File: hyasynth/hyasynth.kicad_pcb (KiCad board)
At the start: 2 copper layers, 43 parts, among them J1 Conn_01x04_Male, J2 Conn_01x03_Male, J3 Conn_01x09_Male, J4 Conn_01x05_Male, SW1 Power Switch, SW10 G# Ab, SW11 A, SW12 A# Bb, SW13 B, SW14 C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

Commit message: started laying out pcb
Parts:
- added J5: Conn_01x02_Male, Connector_PinHeader_2.54mm:PinHeader_1x02_P2.54mm_Vertical, F.Cu at (191.0, 32.0)
- added R5: R, Resistor_SMD:R_0805_2012Metric_Pad1.20x1.40mm_HandSolder, F.Cu at (192.0, 35.0)
- BT1, BT2, C6, C8: moved to B.Cu
- moved J1 243.4 mm to (257.0, 15.2)
- moved SW1 217.1 mm to (258.0, 54.0), turned to 180 degrees
- moved BT1 209.8 mm to (236.0, 38.0), turned to 180 degrees
- moved SW18 209.0 mm to (250.0, 39.0)
- moved J3 200.9 mm to (225.8, 32.0), turned to 90 degrees
- moved SW16 199.2 mm to (249.0, 58.0), turned to 90 degrees
- moved SW13 198.9 mm to (246.0, 82.0), turned to 90 degrees
- moved R1 194.8 mm to (251.0, 33.0)
- moved SW12 194.5 mm to (240.0, 73.0), turned to 90 degrees
- moved SW14 192.7 mm to (256.0, 82.0), turned to 90 degrees
- moved R2 190.3 mm to (255.0, 32.0)
- moved J2 188.7 mm to (210.0, 36.0)
- moved SW9 183.1 mm to (219.0, 82.0), turned to 90 degrees
- moved C2 182.5 mm to (229.0, 46.0), turned to 90 degrees
- moved U1 179.4 mm to (236.0, 43.0)
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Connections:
- C10 pad 2: Net-(C10-Pad2) -> /V_pot_in
- U3 pad 3: Net-(C10-Pad2) -> /V_pot_out
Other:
- board outline added: 100 x 60 mm

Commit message: Did very little work
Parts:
- moved J1 41.6 mm to (219.0, 32.0)
- moved C3 5.06 mm to (222.4, 49.0)
- moved C10 1.51 mm to (198.8, 32.0)
- moved R5 0.42 mm to (192.3, 35.3)
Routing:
- net GND: track 0.00 -> 42.6 mm
- net /A_in: track 0.00 -> 37.0 mm
- net /DAC: track 0.00 -> 30.5 mm
- net /SPK-: track 0.00 -> 13.7 mm
- net /D_in: track 0.00 -> 13.1 mm
- net /SPK+: track 0.00 -> 10.3 mm
- net /V_pot_in: track 0.00 -> 7.66 mm
- net VDD: track 0.00 -> 4.92 mm
- net Net-(C11-Pad2): track 0.00 -> 3.86 mm
- net /V_pot_out: track 0.00 -> 3.42 mm
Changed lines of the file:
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@@
   )
   (setup
+    (stackup
+      (layer "F.SilkS" (type "Top Silk Screen"))
+      (layer "F.Paste" (type "Top Solder Paste"))
+      (layer "F.Mask" (type "Top Solder Mask") (thickness 0.01))
+      (layer "F.Cu" (type "copper") (thickness 0.035))
+      (layer "dielectric 1" (type "core") (thickness 1.51) (material "FR4") (epsilon_r 4.5) (loss_tangent 0.02))
+      (layer "B.Cu" (type "copper") (thickness 0.035))
+      (layer "B.Mask" (type "Bottom Solder Mask") (thickness 0.01))
+      (layer "B.Paste" (type "Bottom Solder Paste"))
+      (layer "B.SilkS" (type "Bottom Silk Screen"))
+      (copper_finish "None")
+      (dielectric_constraints no)
+    )
     (pad_to_mask_clearance 0)
+    (grid_origin 189.2 46.2)
     (pcbplotparams
       (layerselection 0x00010fc_ffffffff)
@@
   )
   (footprint "Connector_PinSocket_2.54mm:PinSocket_1x04_P2.54mm_Vertical" (layer "F.Cu")
-    (at 257.025 15.2)
+    (at 219 32)
     (descr "Through hole straight socket strip, 1x04, 2.54mm pitch, single row (from Kicad 4.0.7), script generated")
     (tags "Through hole socket strip THT 1x04 2.54mm single row")
@@
   )
   (footprint "Capacitor_Tantalum_SMD:CP_EIA-6032-28_Kemet-C_Pad2.25x2.35mm_HandSolder" (layer "F.Cu")
-    (at 225.55 53)
+    (at 222.45 49)
     (descr "Tantalum Capacitor SMD Kemet-C (6032-28 Metric), IPC_7351 nominal, (Body size from: http://www.kemet.com/Lists/ProductCatalog/Attachments/253/KEM_TC101_STD.pdf), generated with kicad-footprint-generator")
     (tags "capacitor tantalum")
@@
   )
   (footprint "Resistor_SMD:R_0805_2012Metric_Pad1.20x1.40mm_HandSolder" (layer "F.Cu")
-    (at 192 35 180)
+    (at 192.3 35.3 180)
     (descr "Resistor SMD 0805 (2012 Metric), square (rectangular) end terminal, IPC_7351 nominal with elongated pad for handsoldering. (Body size source: IPC-SM-782 page 72, https://www.pcb-3d.com/wordpress/wp-content/uploads/ipc-sm-782a_amendment_1_and_2.pdf), generated with kicad-footprint-generator")
     (tags "resistor handsolder")
@@
   )
   (footprint "Capacitor_SMD:C_0805_2012Metric_Pad1.18x1.45mm_HandSolder" (layer "F.Cu")
-    (at 199.9625 33 180)
+    (at 198.8375 32 180)
     (descr "Capacitor SMD 0805 (2012 Metric), square (rectangular) end terminal, IPC_7351 nominal with elongated pad for handsoldering. (Body size source: IPC-SM-782 page 76, https://www.pcb-3d.com/wordpress/wp-content/uploads/ipc-sm-782a_amendment_1_and_2.pdf, https://docs.google.com/spreadsheets/d/1BsfQQcO9C6DZCsRaXUlFlo91Tg2WpOkGARC1WS5S8t0/edit?usp=sharing), generated with kicad-footprint-generator")
     (tags "capacitor handsolder")
@@
   )
   (gr_rect (start 260 30) (end 160 90) (layer "Edge.Cuts") (width 0.1) (fill none))
+  (segment (start 195.382731 40.675) (end 191.7 44.357731) (width 0.2032) (layer "F.Cu") (net 3))
+  (segment (start 189.3 45.3375) (end 185.9625 42) (width 0.2032) (layer "F.Cu") (net 3))
+  (segment (start 196.46 49.3) (end 198.16 51) (width 0.2032) (layer "F.Cu") (net 3))
+  (segment (start 191.348889 52.151111) (end 189.851111 52.151111) (width 0.2032) (layer "F.Cu") (net 3))
+  (segment (start 201 38) (end 198.325 40.675) (width 0.2032) (layer "F.Cu") (net 3))
+  (segment (start 189.3 51.6) (end 189.3 45.3375) (width 0.2032) (layer "F.Cu") (net 3))
+  (segment (start 191.348889 52.151111) (end 193.556807 52.151111) (width 0.2032) (layer "F.Cu") (net 3))
+  (segment (start 196.1125 40.675) (end 195.382731 40.675) (width 0.2032) (layer "F.Cu") (net 3))
+  (segment (start 191.7 44.357731) (end 191.7 51.8) (width 0.2032) (layer "F.Cu") (net 3))
+  (segment (start 194.231111 51.476807) (end 194.231111 50.168889) (width 0.2032) (layer "F.Cu") (net 3))
+  (segment (start 191.7 51.8) (end 191.348889 52.151111) (width 0.2032) (layer "F.Cu") (net 3))
+  (segment (start 193.556807 52.151111) (end 194.231111 51.476807) (width 0.2032) (layer "F.Cu") (net 3))
+  (segment (start 195.1 49.3) (end 196.46 49.3) (width 0.2032) (layer "F.Cu") (net 3))
+  (segment (start 189.851111 52.151111) (end 189.3 51.6) (width 0.2032) (layer "F.Cu") (net 3))
+  (segment (start 194.231111 50.168889) (end 195.1 49.3) (width 0.2032) (layer "F.Cu") (net 3))
+  (segment (start 198.325 40.675) (end 196.1125 40.675) (width 0.2032) (layer "F.Cu") (net 3))
+  (segment (start 196.1875 41.25) (end 196.1125 41.325) (width 0.2032) (layer "F.Cu") (net 25))
+  (segment (start 201 41.25) (end 196.1875 41.25) (width 0.2032) (layer "F.Cu") (net 25))
+  (segment (start 201.4 47.14) (end 201.4 50.3) (width 0.2032) (layer "F.Cu") (net 26))
+  (segment (start 210 38.54) (end 201.4 47.14) (width 0.2032) (layer "F.Cu") (net 26))
+  (segment (start 198.9 52.8) (end 189.8 52.8) (width 0.2032) (layer "F.Cu") (net 26))
+  (segment (start 201.4 50.3) (end 198.9 52.8) (width 0.2032) (layer "F.Cu") (net 26))
+  (segment (start 189.8 52.8) (end 188 51) (width 0.2032) (layer "F.Cu") (net 26))
+  (segment (start 210 41.08) (end 210 43.1) (width 0.2032) (layer "F.Cu") (net 33))
+  (segment (start 210 43.1) (end 199.5 53.6) (width 0.2032) (layer "F.Cu") (net 33))
+  (segment (start 199.5 53.6) (end 181.6 53.6) (width 0.2032) (layer "F.Cu") (net 33))
+  (segment (start 181.6 53.6) (end 180 52) (width 0.2032) (layer "F.Cu") (net 33))
+  (segment (start 210 33.8) (end 210 36) (width 0.2032) (layer "F.Cu") (net 36))
+  (segment (start 199.875 32) (end 208.2 32) (width 0.2032) (layer "F.Cu") (net 36))
+  (segment (start 208.2 32) (end 210 33.8) (width 0.2032) (layer "F.Cu") (net 36))
+  (segment (start 193.54 32) (end 197.8 32) (width 0.508) (layer "F.Cu") (net 37))
+  (segment (start 193.54 35.06) (end 193.3 35.3) (width 0.508) (layer "F.Cu") (net 37))
+  (segment (start 193.54 32) (end 193.54 35.06) (width 0.508) (layer "F.Cu") (net 37))
+  (segment (start 191.8875 41.975) (end 188.0625 41.975) (width 0.2032) (layer "F.Cu") (net 38))
+  (segment (start 188.0625 41.975) (end 188.0375 42) (width 0.2032) (layer "F.Cu") (net 38))
+  (segment (start 190.54 44.867731) (end 190.54 51) (width 0.2032) (layer "F.Cu") (net 39))
+  (segment (start 196.1125 40.025) (end 195.382731 40.025) (width 0.2032) (layer "F.Cu") (net 39))
+  (segment (start 195.382731 40.025) (end 190.54 44.867731) (width 0.2032) (layer "F.Cu") (net 39))
+  (segment (start 193.08 51) (end 193.08 45.0075) (width 0.2032) (layer "F.Cu") (net 40))
+  (segment (start 193.08 45.0075) (end 196.1125 41.975) (width 0.2032) (layer "F.Cu") (net 40))
+  (segment (start 191 35) (end 191.3 35.3) (width 0.508) (layer "F.Cu") (net 48))
+  (segment (start 191 32) (end 191 35) (width 0.508) (layer "F.Cu") (net 48))
 )

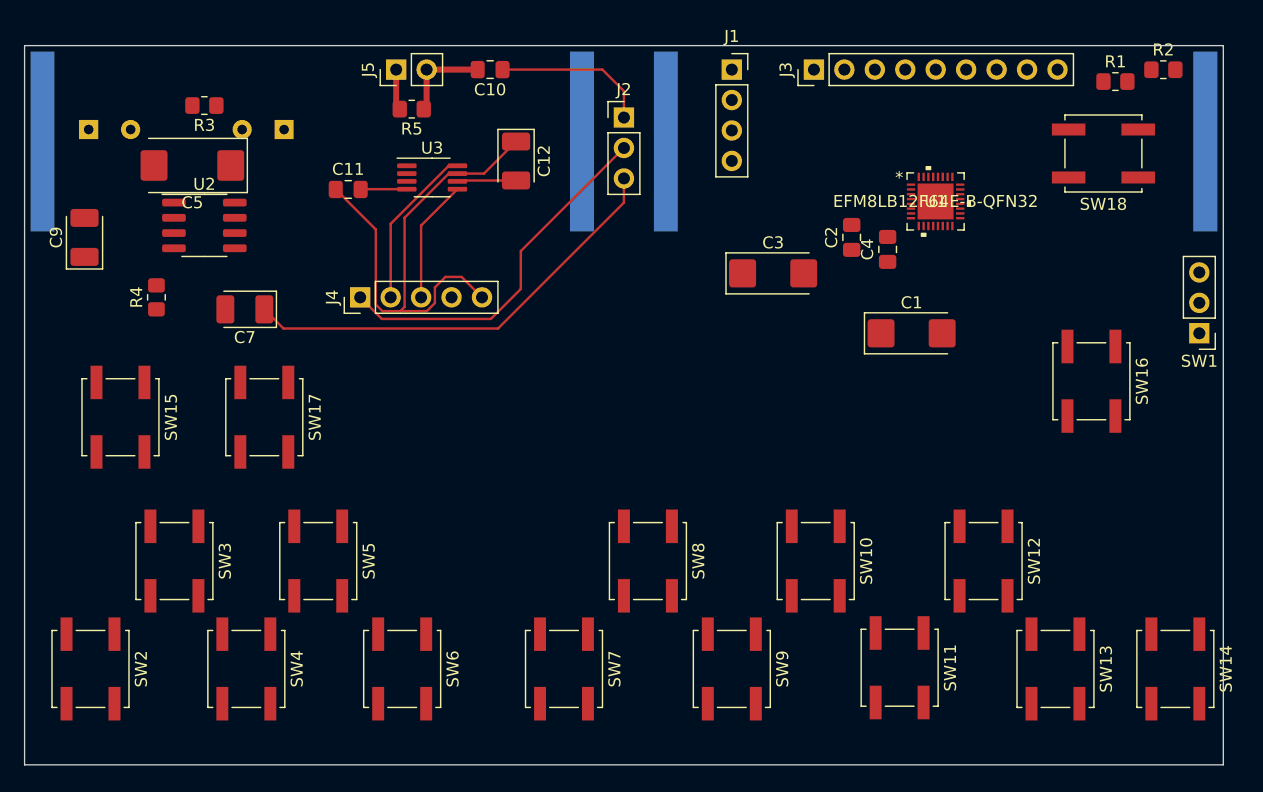
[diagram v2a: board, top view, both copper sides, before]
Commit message: set battery positions, adjusted for caps
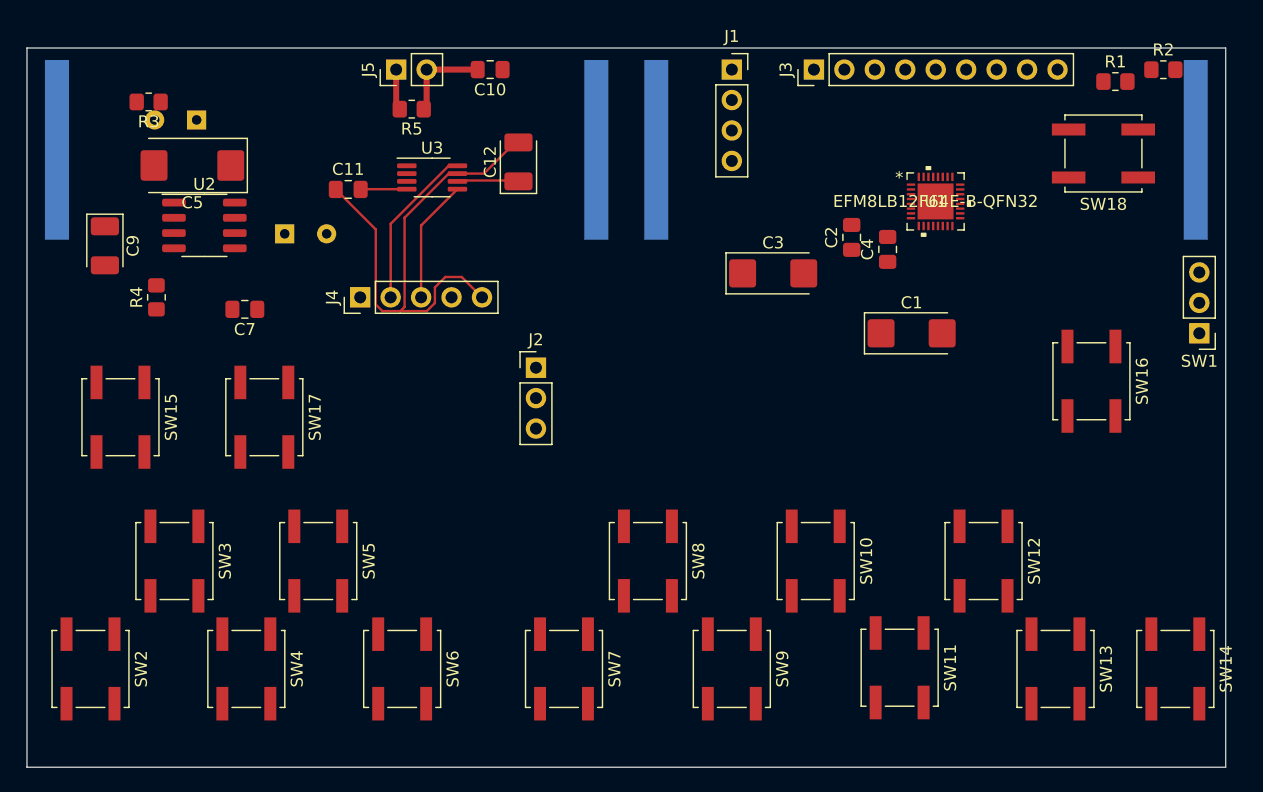
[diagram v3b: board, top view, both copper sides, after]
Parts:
- C12, C9: footprint Capacitor_Tantalum_SMD:CP_EIA-3528-21_Kemet-B_Pad1.50x2.35mm_HandSolder -> Capacitor_Tantalum_SMD:CP_EIA-3528-12_Kemet-T_Pad1.50x2.35mm_HandSolder
- C7: value 1u -> 0.1u; footprint Capacitor_Tantalum_SMD:CP_EIA-3528-21_Kemet-B_Pad1.50x2.35mm_HandSolder -> Capacitor_SMD:C_0805_2012Metric_Pad1.18x1.45mm_HandSolder
- moved J2 22.1 mm to (202.7, 56.9)
- moved C8 18.5 mm to (181.7, 45.7)
- moved C6 7.34 mm to (174.4, 36.2)
- moved R3 4.66 mm to (170.4, 34.7)
- moved C9 1.84 mm to (166.7, 46.7), turned to -90 degrees
- moved BT2 1.39 mm to (185.2, 38.7)
- moved BT1 1.06 mm to (235.2, 38.7)
- moved C12 0.21 mm to (201.2, 39.7), turned to 90 degrees
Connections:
- C12 pad 1: GND -> VDD
- C12 pad 2: VDD -> GND
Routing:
- net /A_in: track 37.0 -> 0.00 mm
- net /DAC: track 30.5 -> 0.00 mm
- net /D_in: track 13.1 -> 0.00 mm

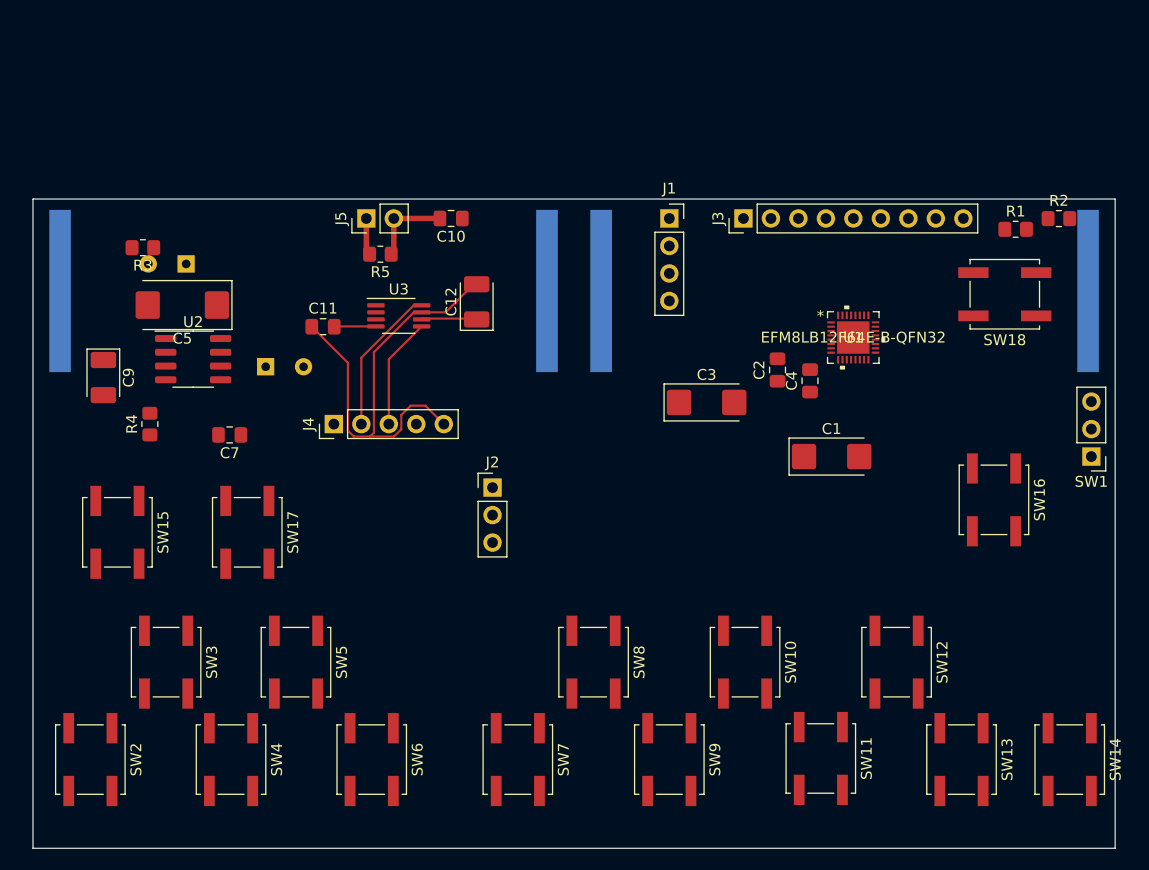
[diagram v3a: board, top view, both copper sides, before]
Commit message: laid out switches, started routing them.
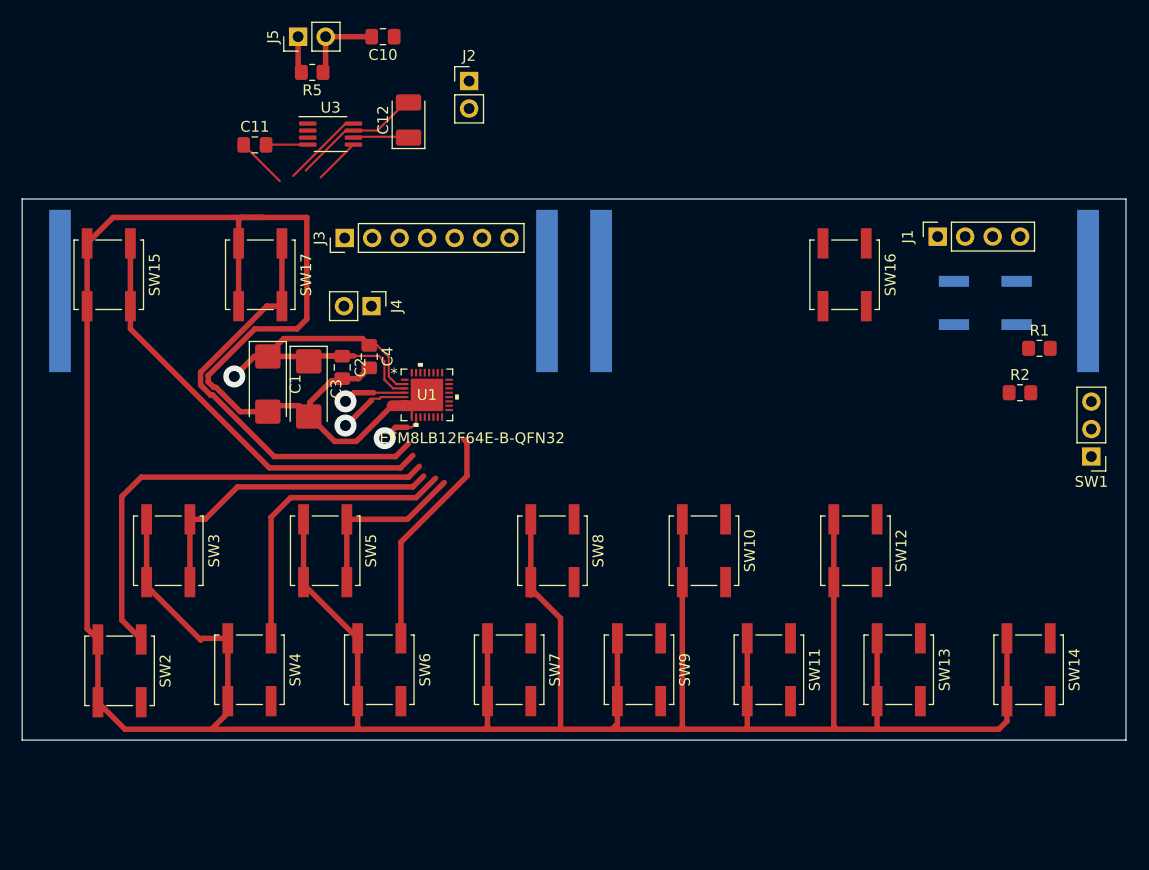
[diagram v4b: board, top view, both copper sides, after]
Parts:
- removed C5: 10u, Capacitor_Tantalum_SMD:CP_EIA-7343-31_Kemet-D_Pad2.25x2.55mm_HandSolder
- removed C6: 47u, Capacitor_THT:CP_Radial_D8.0mm_P3.50mm
- removed C7: 0.1u, Capacitor_SMD:C_0805_2012Metric_Pad1.18x1.45mm_HandSolder
- removed C8: 330u, Capacitor_THT:CP_Radial_D8.0mm_P3.50mm
- removed C9: 1u, Capacitor_Tantalum_SMD:CP_EIA-3528-12_Kemet-T_Pad1.50x2.35mm_HandSolder
- removed R3: 100k, Resistor_SMD:R_0805_2012Metric_Pad1.20x1.40mm_HandSolder
- removed R4: R, Resistor_SMD:R_0805_2012Metric_Pad1.20x1.40mm_HandSolder
- removed U2: BH3544F, Package_SO:SOP-8_3.76x4.96mm_P1.27mm
- J2: value Conn_01x03_Male -> Conn_01x02_Male; footprint Connector_PinHeader_2.54mm:PinHeader_1x03_P2.54mm_Vertical -> Connector_PinHeader_2.54mm:PinHeader_1x02_P2.54mm_Vertical
- J3: value Conn_01x09_Male -> Conn_01x07_Male; footprint Connector_PinHeader_2.54mm:PinHeader_1x09_P2.54mm_Vertical -> Connector_PinHeader_2.54mm:PinHeader_1x07_P2.54mm_Vertical
- J4: value Conn_01x05_Male -> Conn_01x02_Male; footprint Connector_PinHeader_2.54mm:PinHeader_1x05_P2.54mm_Vertical -> Connector_PinHeader_2.54mm:PinHeader_1x02_P2.54mm_Vertical
- SW18: moved to B.Cu
- moved C1 52.5 mm to (181.9, 47.3), turned to -90 degrees
- moved C4 40.8 mm to (191.3, 44.8), turned to -90 degrees
- moved C2 40.2 mm to (188.8, 45.8), turned to -90 degrees
- moved U1 39.8 mm to (196.6, 48.3)
- moved J2 37.6 mm to (200.5, 19.3)
- moved J3 36.9 mm to (189.0, 33.8)
- moved C3 36.8 mm to (185.7, 47.7), turned to -90 degrees
- moved SW16 25.0 mm to (235.2, 37.2)
- moved J1 24.9 mm to (243.8, 33.7), turned to 90 degrees
- moved SW17 23.8 mm to (181.2, 37.2)
- moved SW15 23.8 mm to (167.2, 37.2)
- moved C10 17.9 mm to (192.5, 15.2)
- moved C11 17.9 mm to (180.7, 25.2)
- moved J5 17.9 mm to (184.7, 15.2)
- moved U3 17.9 mm to (187.7, 24.2)
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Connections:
- C10 pad 1: /D_in -> /DAC
- J2 pad 1: /D_in -> /SPK-
- J2 pad 2: /DAC -> /SPK+
- J3 pad 1: VDD -> /GPIO_4
- J3 pad 2: /GPIO_4 -> /GPIO_3
- J3 pad 3: /GPIO_3 -> /GPIO_2
- J3 pad 4: /GPIO_2 -> /GPIO_1
- J3 pad 5: /GPIO_1 -> /Uart_TX
- J3 pad 6: /Uart_TX -> /Uart_RX
- J3 pad 7: /Uart_RX -> /GPIO_0
- J4 pad 1: /DAC -> VDD
- J4 pad 2: /SPK- -> GND
- U1 pad 11: /Down -> /Up
- U1 pad 12: /Up -> /Down
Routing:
- net GND: track 42.6 -> 381.2 mm
- net /Low_C: track 0.00 -> 42.6 mm
- net /Down: track 0.00 -> 39.8 mm
- net /Up: track 0.00 -> 39.5 mm
- net VDD: track 4.92 -> 40.7 mm, vias 0 -> 1
- net /C#: track 0.00 -> 29.1 mm
- net /D: track 0.00 -> 27.9 mm
- net /E: track 0.00 -> 21.1 mm
- net /D#: track 0.00 -> 16.2 mm
- net /C2D: track 0.00 -> 6.56 mm, vias 0 -> 1
- net /SPK-: track 13.7 -> 7.58 mm
- net /SPK+: track 10.3 -> 4.29 mm
- net /C2CLK: track 0.00 -> 5.81 mm, vias 0 -> 1
- net /DAC: track 0.00 -> 4.14 mm, vias 0 -> 1
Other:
- board size 100 x 60 mm -> 102 x 50 mm
